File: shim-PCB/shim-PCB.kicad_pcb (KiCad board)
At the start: 4 copper layers, 67.5 x 95.4 mm, 26 parts, among them J1 ROMI-Encoder, J10 LineSensor, J11 LineSensor, J12 SPI, J13 Ultrasonic., J14 THING, J15 THING, J16 Conn_01x02_Female, J17 i2c, J2 ROMI-Encoder, J3 Conn_01x19_Female, J4 ServoAnalog, J5 Conn_01x19_Female, J6 Conn_01x19_Female, J7 ROMI, J8 ROMI, J9 Conn_01x19_Female

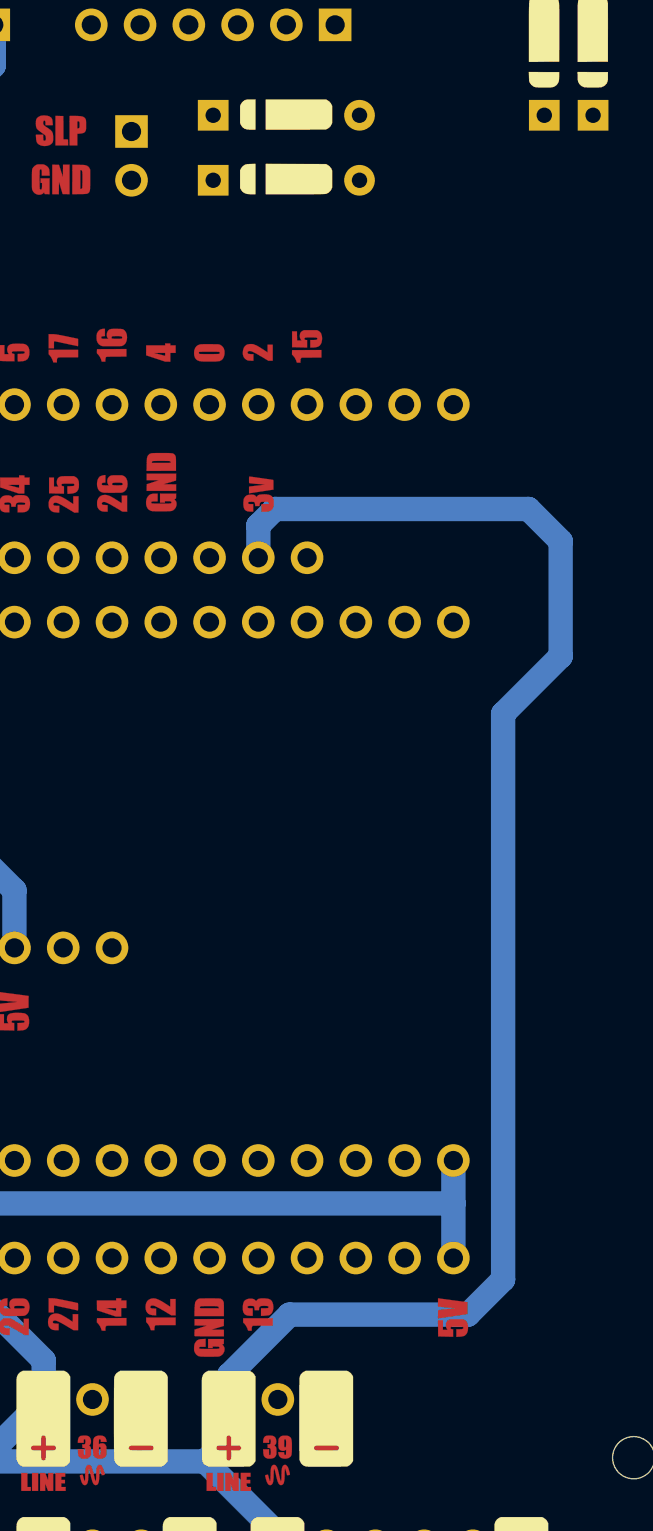
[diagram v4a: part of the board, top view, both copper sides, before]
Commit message: Moved gnd-slp jumper
#19
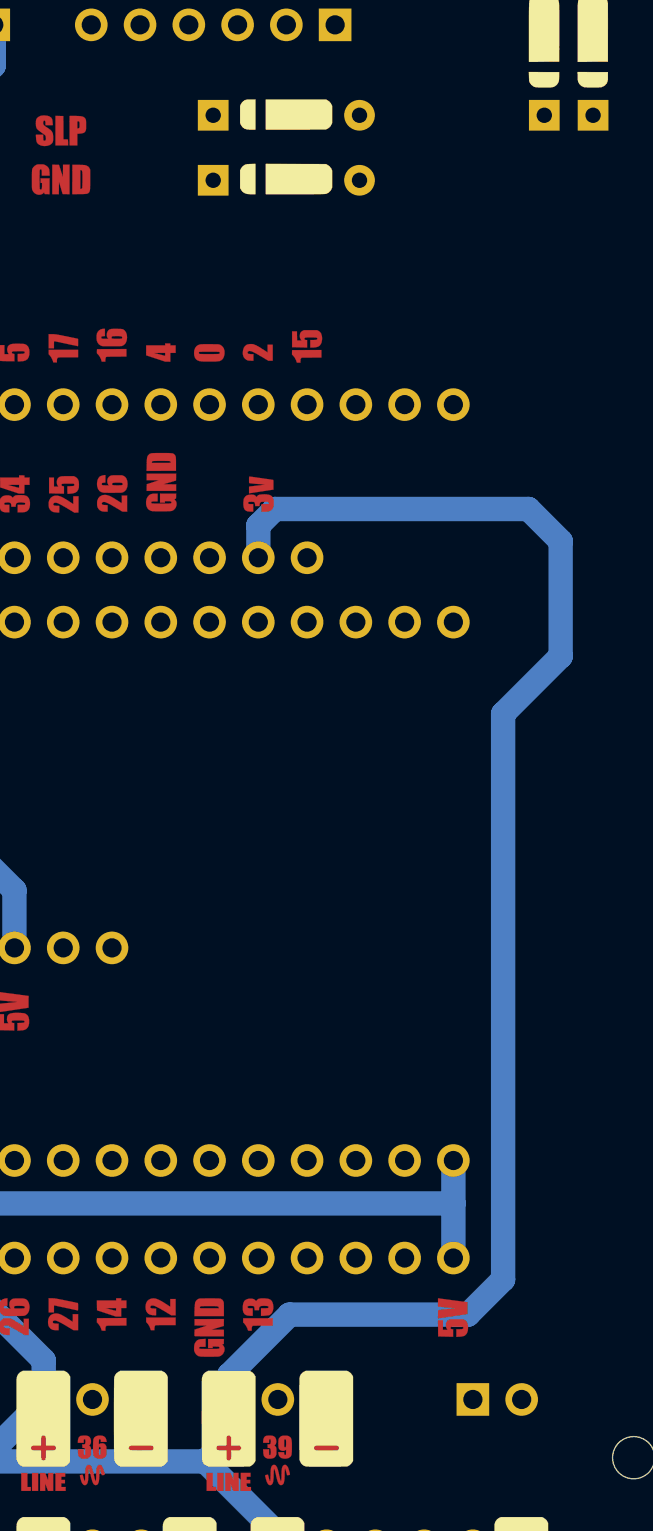
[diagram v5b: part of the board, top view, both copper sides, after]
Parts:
- moved J16 68.4 mm to (157.5, 129.5), turned to 90 degrees
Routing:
- net GPIO5: track 83.8 -> 80.6 mm
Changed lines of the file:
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@@
     (thickness 1.6)
     (drawings 162)
-    (tracks 326)
+    (tracks 325)
     (zones 0)
     (modules 26)
@@
   )
   (module Connector_PinSocket_2.54mm:PinSocket_1x02_P2.54mm_Vertical (layer F.Cu)
-    (at 139.7 63.5)
+    (at 157.48 129.54 90)
     (descr "Through hole straight socket strip, 1x02, 2.54mm pitch, single row (from Kicad 4.0.7), script generated")
     (tags "Through hole socket strip THT 1x02 2.54mm single row")
-    (fp_text reference J16 (at 0 -2.77) (layer F.SilkS) hide
+    (fp_text reference J16 (at 0 -2.77 90) (layer F.SilkS) hide
       (effects (font (size 1 1) (thickness 0.15)))
     )
-    (fp_text value Conn_01x02_Female (at 0 5.31) (layer F.Fab)
+    (fp_text value Conn_01x02_Female (at 0 5.31 90) (layer F.Fab)
       (effects (font (size 1 1) (thickness 0.15)))
     )
-    (pad 1 thru_hole rect (at 0 0) (size 1.7 1.7) (drill 1) (layers *.Cu *.Mask)
+    (pad 1 thru_hole rect (at 0 0 90) (size 1.7 1.7) (drill 1) (layers *.Cu *.Mask)
       (net 33 GPIO15))
-    (pad 2 thru_hole oval (at 0 2.54) (size 1.7 1.7) (drill 1) (layers *.Cu *.Mask)
+    (pad 2 thru_hole oval (at 0 2.54 90) (size 1.7 1.7) (drill 1) (layers *.Cu *.Mask)
       (net 1 GND))
     (model ${KISYS3DMOD}/Connector_PinSocket_2.54mm.3dshapes/PinSocket_1x02_P2.54mm_Vertical.wrl
@@
   (segment (start 147.4794 123.5239) (end 154.94 130.9845) (width 0.25) (layer In1.Cu) (net 5))
   (segment (start 154.94 130.9845) (end 154.94 137.16) (width 0.25) (layer In1.Cu) (net 5) (status 20))
+  (segment (start 173.905 57.5644) (end 173.6264 57.5644) (width 0.1524) (layer In1.Cu) (net 7) (status 30))
   (segment (start 115.824 117.094) (end 124.714 108.204) (width 0.25) (layer In2.Cu) (net 12) (status 10))
   (segment (start 124.714 108.204) (end 124.714 93.2805) (width 0.25) (layer In2.Cu) (net 12))
@@
   (segment (start 147.574 77.315) (end 154.0055 70.8835) (width 0.25) (layer In1.Cu) (net 19))
   (segment (start 154.0055 70.8835) (end 155.5109 70.8835) (width 0.25) (layer In1.Cu) (net 19))
+  (segment (start 163.74 62.6544) (end 163.74 61.3018) (width 0.25) (layer In1.Cu) (net 19))
+  (segment (start 163.74 61.3018) (end 162.687 60.2488) (width 0.25) (layer In1.Cu) (net 19))
+  (segment (start 162.687 60.2488) (end 160.6804 60.2488) (width 0.25) (layer In1.Cu) (net 19))
+  (segment (start 159.4125 61.5167) (end 159.4125 66.9819) (width 0.25) (layer In1.Cu) (net 19))
+  (segment (start 160.6804 60.2488) (end 159.4125 61.5167) (width 0.25) (layer In1.Cu) (net 19))
+  (segment (start 155.5109 70.8835) (end 159.4125 66.9819) (width 0.25) (layer In1.Cu) (net 19))
+  (segment (start 171.373 62.6364) (end 171.355 62.6544) (width 0.25) (layer In1.Cu) (net 19))
+  (segment (start 173.9138 62.6364) (end 171.373 62.6364) (width 0.25) (layer In1.Cu) (net 19))
   (segment (start 136.144 120.9974) (end 136.144 122.174) (width 0.25) (layer In2.Cu) (net 20) (status 20))
   (segment (start 136.144 117.094) (end 136.144 120.9974) (width 0.25) (layer In2.Cu) (net 20) (status 10))
@@
   (segment (start 136.144 117.094) (end 125.984 106.934) (width 0.25) (layer In1.Cu) (net 20) (status 10))
   (segment (start 125.984 106.934) (end 125.984 106.02) (width 0.25) (layer In1.Cu) (net 20) (status 20))
-  (segment (start 173.905 57.5644) (end 173.6264 57.5644) (width 0.1524) (layer In1.Cu) (net 7) (status 30))
-  (segment (start 163.74 62.6544) (end 163.74 61.3018) (width 0.25) (layer In1.Cu) (net 19))
-  (segment (start 163.74 61.3018) (end 162.687 60.2488) (width 0.25) (layer In1.Cu) (net 19))
-  (segment (start 162.687 60.2488) (end 160.6804 60.2488) (width 0.25) (layer In1.Cu) (net 19))
-  (segment (start 159.4125 61.5167) (end 159.4125 66.9819) (width 0.25) (layer In1.Cu) (net 19))
-  (segment (start 160.6804 60.2488) (end 159.4125 61.5167) (width 0.25) (layer In1.Cu) (net 19))
-  (segment (start 155.5109 70.8835) (end 159.4125 66.9819) (width 0.25) (layer In1.Cu) (net 19))
-  (segment (start 171.373 62.6364) (end 171.355 62.6544) (width 0.25) (layer In1.Cu) (net 19))
-  (segment (start 173.9138 62.6364) (end 171.373 62.6364) (width 0.25) (layer In1.Cu) (net 19))
   (segment (start 161.2 62.6544) (end 161.2 63.6132) (width 0.25) (layer In1.Cu) (net 20))
   (segment (start 162.7632 65.1764) (end 173.9138 65.1764) (width 0.25) (layer In1.Cu) (net 20))
@@
   (segment (start 133.604 87.3628) (end 133.604 89.0524) (width 0.25) (layer In2.Cu) (net 30) (status 20))
   (segment (start 157.48 137.16) (end 157.48 131.2873) (width 0.25) (layer In1.Cu) (net 30) (status 10))
-  (segment (start 157.48 131.2873) (end 155.2522 129.0595) (width 0.25) (layer In1.Cu) (net 30))
   (segment (start 155.2522 129.0595) (end 155.2522 110.7006) (width 0.25) (layer In1.Cu) (net 30))
   (segment (start 155.2522 110.7006) (end 133.604 89.0524) (width 0.25) (layer In1.Cu) (net 30) (status 20))

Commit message: Rotate Ultrasonic 180 degrees
#21
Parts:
- moved J13 7.62 mm to (131.1, 137.2), turned to 270 degrees
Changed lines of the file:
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@@
   )
   (module Connector_PinSocket_2.54mm:PinSocket_1x04_P2.54mm_Vertical (layer F.Cu)
-    (at 123.444 137.16 90)
+    (at 131.064 137.16 270)
     (descr "Through hole straight socket strip, 1x04, 2.54mm pitch, single row (from Kicad 4.0.7), script generated")
     (tags "Through hole socket strip THT 1x04 2.54mm single row")
@@
       (effects (font (size 1 1) (thickness 0.15)))
     )
-    (pad 1 thru_hole rect (at 0 0 90) (size 1.7 1.7) (drill 1) (layers *.Cu *.Mask)
+    (pad 1 thru_hole rect (at 0 0 270) (size 1.7 1.7) (drill 1) (layers *.Cu *.Mask)
       (net 34 +3V3))
-    (pad 2 thru_hole oval (at 0 2.54 90) (size 1.7 1.7) (drill 1) (layers *.Cu *.Mask)
+    (pad 2 thru_hole oval (at 0 2.54 270) (size 1.7 1.7) (drill 1) (layers *.Cu *.Mask)
       (net 16 GPIO32))
-    (pad 3 thru_hole oval (at 0 5.08 90) (size 1.7 1.7) (drill 1) (layers *.Cu *.Mask)
+    (pad 3 thru_hole oval (at 0 5.08 270) (size 1.7 1.7) (drill 1) (layers *.Cu *.Mask)
       (net 21 GPIO14))
-    (pad 4 thru_hole oval (at 0 7.62 90) (size 1.7 1.7) (drill 1) (layers *.Cu *.Mask)
+    (pad 4 thru_hole oval (at 0 7.62 270) (size 1.7 1.7) (drill 1) (layers *.Cu *.Mask)
       (net 1 GND))
     (model ${KISYS3DMOD}/Connector_PinSocket_2.54mm.3dshapes/PinSocket_1x04_P2.54mm_Vertical.wrl

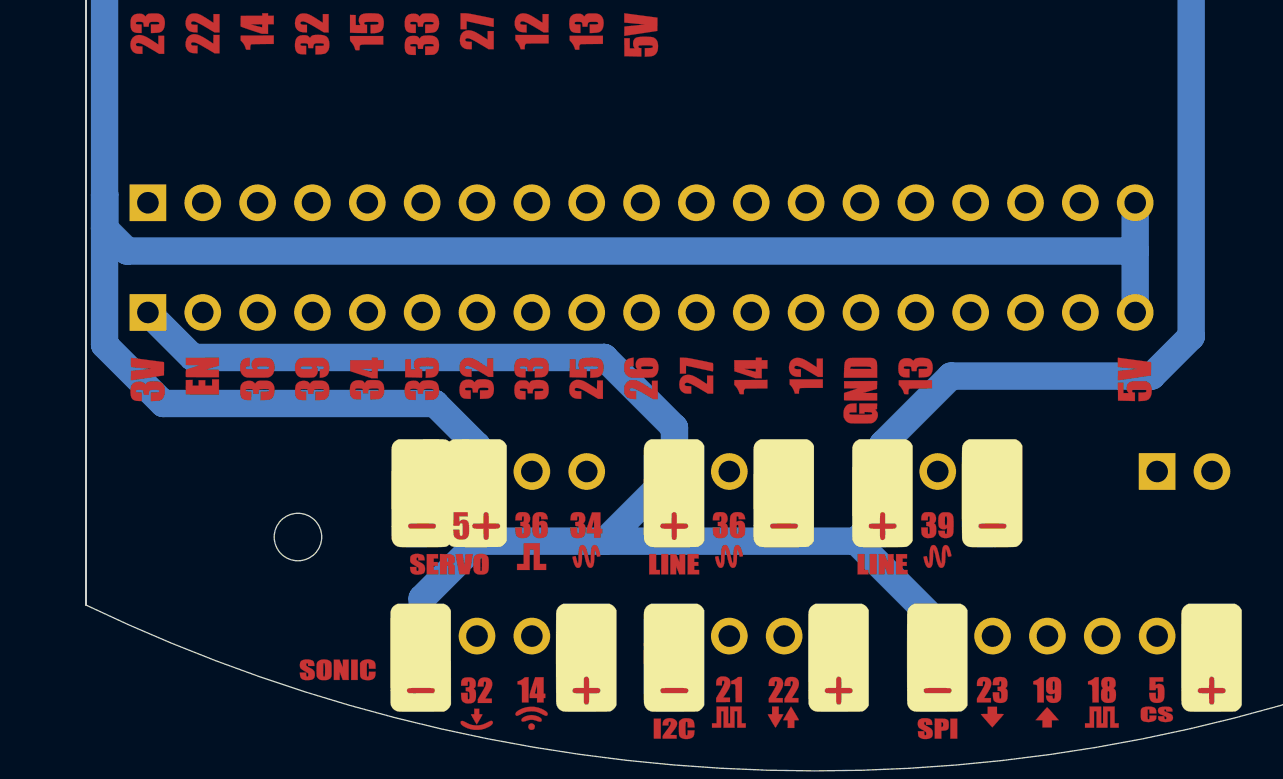
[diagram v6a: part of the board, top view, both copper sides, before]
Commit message: made devkitc footprint shorter by 0.1"
#18
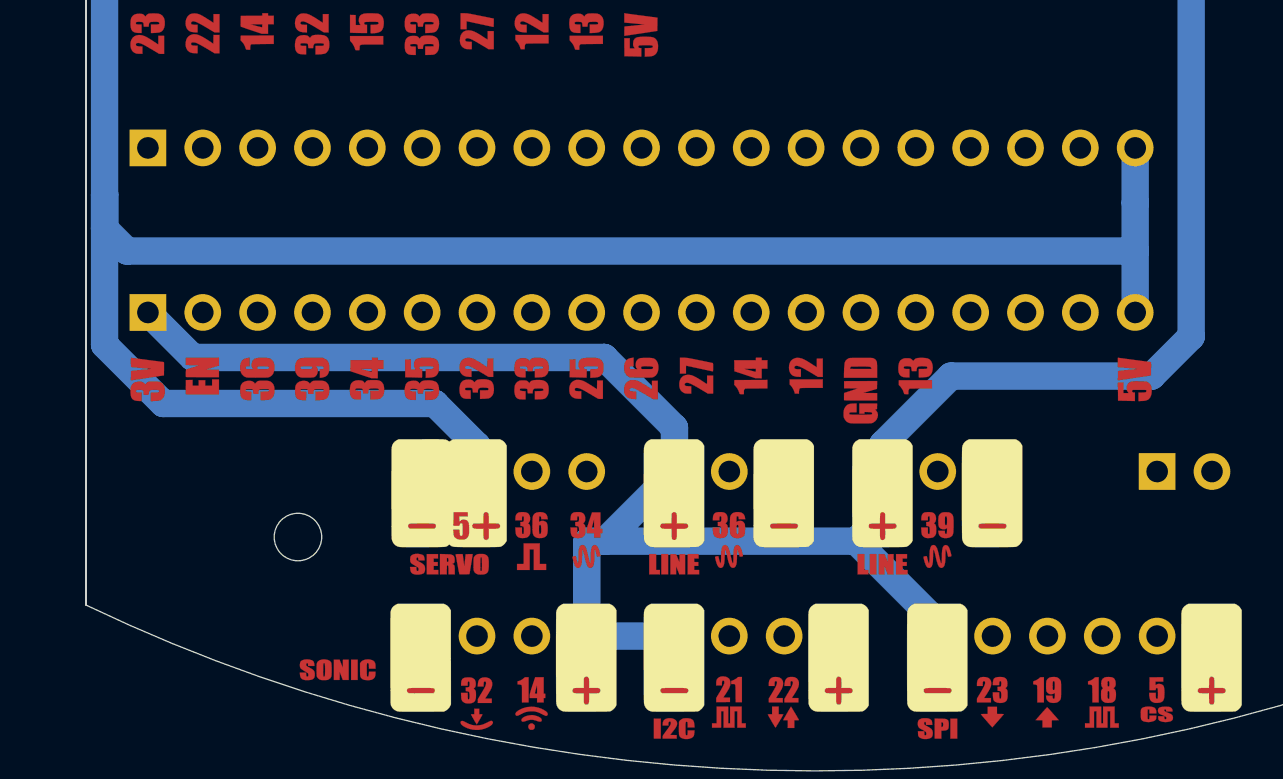
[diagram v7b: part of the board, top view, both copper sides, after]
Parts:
- moved J5 2.54 mm to (110.7, 114.6)
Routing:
- net GPIO27: track 113.6 -> 0.00 mm
- net GPIO21: track 95.4 -> 0.00 mm
- net GPIO15: track 91.0 -> 0.00 mm
- net GPIO26: track 90.8 -> 0.00 mm
- net GPIO12: track 89.8 -> 0.00 mm
- net GPIO23: track 88.1 -> 0.00 mm
- net GPIO13: track 87.6 -> 0.00 mm
- net GPIO19: track 85.2 -> 0.00 mm
- net GPIO34: track 84.2 -> 0.00 mm
- net GPIO18: track 83.8 -> 0.00 mm
- net GPIO5: track 80.6 -> 0.00 mm
- net GPIO22: track 79.3 -> 0.00 mm
- net GPIO39: track 73.7 -> 0.00 mm
- net GPIO17: track 72.4 -> 0.00 mm
- net GPIO25: track 68.0 -> 0.00 mm
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
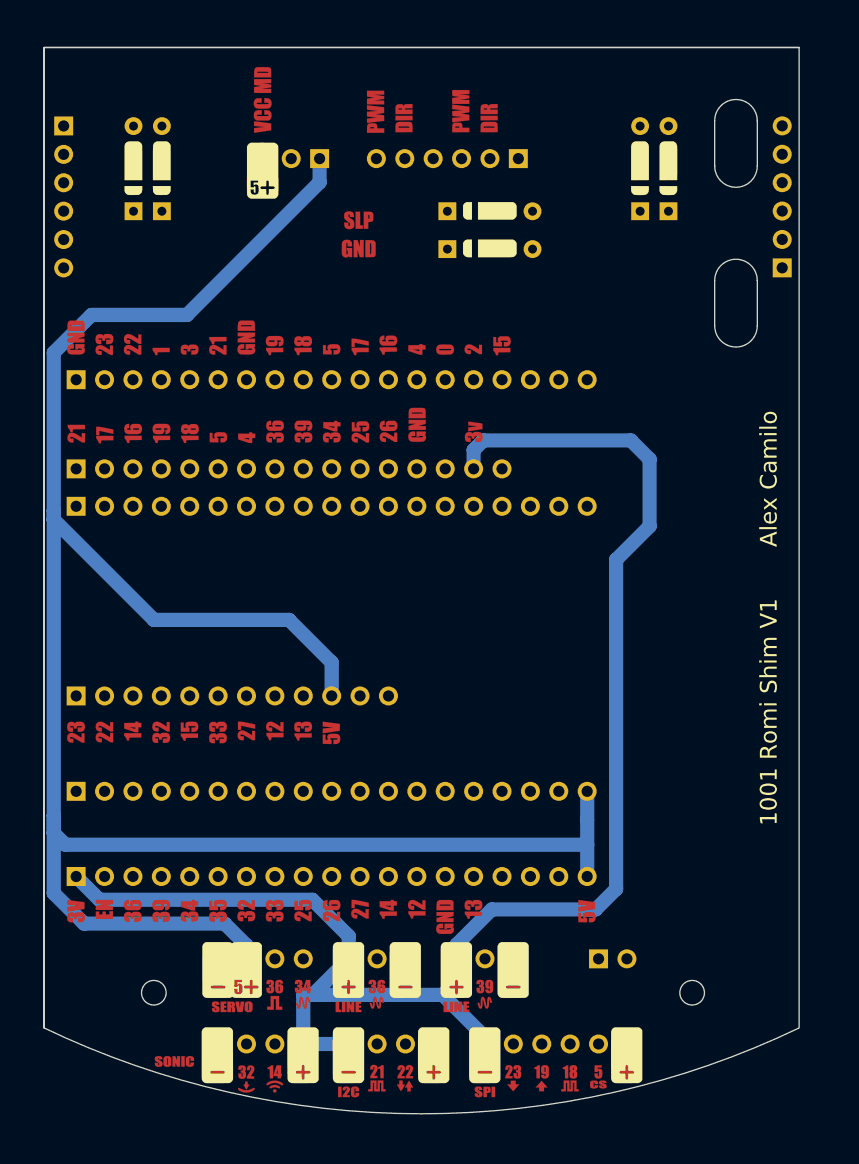
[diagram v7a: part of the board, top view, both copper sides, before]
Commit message: fixed silkscreen, routed board.
#23 #22
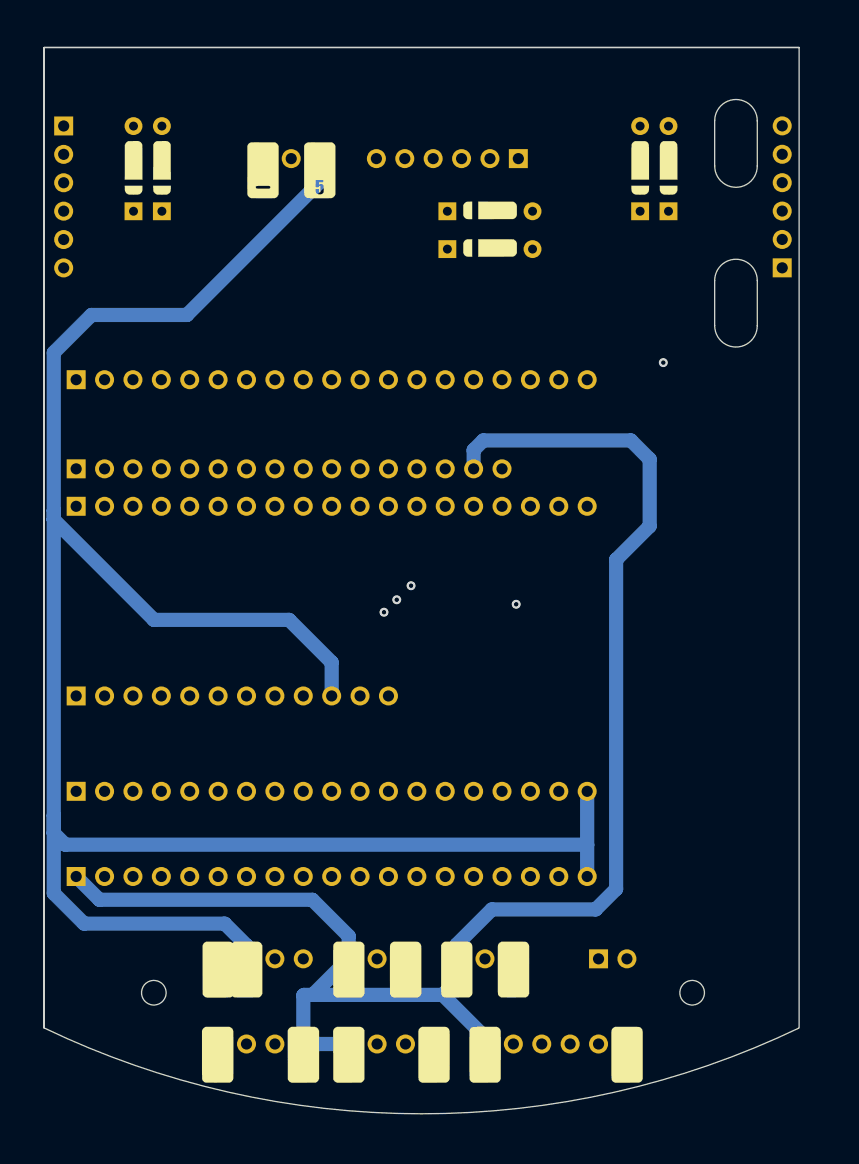
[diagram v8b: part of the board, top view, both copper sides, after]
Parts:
- moved Ref** 2.37 mm to (151.2, 95.1)
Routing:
- net GPIO15: track 0.00 -> 122.2 mm
- net GPIO12: track 0.00 -> 113.4 mm, vias 0 -> 1
- net GPIO34: track 0.00 -> 99.1 mm
- net GPIO27: track 0.00 -> 95.1 mm
- net GPIO23: track 0.00 -> 94.0 mm
- net GPIO21: track 0.00 -> 93.2 mm
- net GPIO26: track 0.00 -> 87.0 mm
- net GPIO19: track 0.00 -> 84.0 mm, vias 0 -> 1
- net GPIO13: track 0.00 -> 82.7 mm, vias 0 -> 1
- net GPIO5: track 0.00 -> 81.9 mm, vias 0 -> 1
- net GPIO18: track 0.00 -> 81.9 mm, vias 0 -> 1
- net GPIO22: track 0.00 -> 79.2 mm
- net GPIO39: track 0.00 -> 76.2 mm
- net GPIO25: track 0.00 -> 72.6 mm
- net GPIO16: track 0.00 -> 72.0 mm
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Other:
- board text removed: "1001 Romi Shim V1 Alex Camilo"
